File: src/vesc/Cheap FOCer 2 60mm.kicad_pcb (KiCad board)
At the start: 2 copper layers, 59.1 x 99.9 mm, 193 parts, among them J1 Conn_01x02, J2 Conn_01x07, J3 Conn_01x03, J4 On/Off, J5 UNUSED MCU PINS, J6 Conn_01x03, P1 MOTOR1, P2 MOTOR1, P3 MOTOR1, P4 HALL/Encoder, P5 SWD, Q1 NCEP60T20, Q2 NCEP60T20, Q3 NCEP60T20, Q4 NCEP60T20, Q5 NCEP60T20, Q6 NCEP60T20, U1 AMS1117-3.3, U2 DRV8301, U3 TP2604-SR, U4 TJA1051T/3/1J, U5 STM32F405RGT6, U6 BMI160, X1 8MHz 10ppm (X50328MSB2GI)

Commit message: routing
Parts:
- removed C10, C11, C9: 22uF, Capacitor_SMD:C_0805_2012Metric
- removed C20, C21, C22: 22uf, Capacitor_SMD:C_0805_2012Metric
- removed C25: 2.2uF, Capacitor_SMD:C_0603_1608Metric
- removed C43: 0.1u, Capacitor_SMD:C_0603_1608Metric
- removed C44: 1nF, Capacitor_SMD:C_0603_1608Metric
- removed C54: 2.2u, Capacitor_SMD:C_0603_1608Metric
- removed C60, C64: 100n, Capacitor_SMD:C_0603_1608Metric
- removed D1, D2: SMF05CT1G, Package_TO_SOT_SMD:SOT-363_SC-70-6
- removed D6: 100v, 1A, Diode_SMD:D_SMA
- removed H3: SLJ, shapes3D:Sam_J
- removed H7: MountingHole, MountingHole:MountingHole_3.2mm_M3_ISO14580_Pad
- removed J2: Conn_01x07, Connector_JST:JST_PH_B7B-PH-K_1x07_P2.00mm_Vertical
- removed J4: On/Off, Connector_JST:JST_PH_B2B-PH-K_1x02_P2.00mm_Vertical
- removed J5: UNUSED MCU PINS, Connector_PinHeader_2.00mm:PinHeader_2x05_P2.00mm_Vertical
- removed J6: Conn_01x03, Connector_PinHeader_2.54mm:PinHeader_1x02_P2.54mm_Vertical
- removed NEG3: MOTOR3, CRF1:1pin_4mm
- removed NTC1: NTC 10k, Resistor_SMD:R_0603_1608Metric
- removed P5: SWD, Connector_PinHeader_2.54mm:PinHeader_1x05_P2.54mm_Vertical
- removed POS1: POS, CRF1:1pin_4mm
- removed R21: 18k, Resistor_SMD:R_0603_1608Metric
- removed R40, R68, R71, R72: DNP, Resistor_SMD:R_0603_1608Metric
- removed R5, R7, R9: 100R, Resistor_SMD:R_0603_1608Metric
- removed R62, R63: 60, Resistor_SMD:R_0603_1608Metric
- removed R64, R65: 20k, Resistor_SMD:R_0603_1608Metric
- removed U4: TJA1051T/3/1J, Package_SO:SOIC-8_3.9x4.9mm_P1.27mm
- removed U6: BMI160, Package_LGA:Bosch_LGA-14_3x2.5mm_P0.5mm
- removed USB1: USB Micro U-D-M5DD-W-1, Connector_USB:USB_Micro-B_Wuerth_614105150721_Vertical
- added C201: 220n, Capacitor_SMD:C_0402_1005Metric, F.Cu at (159.6, 158.7)
- added D101: 5V, Package_TO_SOT_SMD:SOT-523, F.Cu at (156.8, 145.8)
- added D102: 5V, Package_TO_SOT_SMD:SOT-523, F.Cu at (122.5, 158.1)
- added D105: 3V3, Package_DFN_QFN:Diodes_UDFN-10_1.0x2.5mm_P0.5mm, F.Cu at (148.9, 159.1)
- added D210: 30V, Diode_SMD:D_SMF, F.Cu at (125.7, 129.9)
- added D501: 3V3, Package_DFN_QFN:Diodes_UDFN-10_1.0x2.5mm_P0.5mm, F.Cu at (121.0, 145.0)
- added D601: D_Schottky, Diode_SMD:D_SOD-123, F.Cu at (128.9, 112.4)
- added J101: USB_C_Receptacle_USB2.0_16P, Connector_USB:USB_C_Receptacle_GCT_USB4110, F.Cu at (122.3, 164.7)
- added J7: Conn_02x03_Odd_Even, Connector_PinHeader_1.27mm:PinHeader_2x03_P1.27mm_Vertical_SMD, F.Cu at (119.6, 151.6)
- added R501: 10k, Resistor_SMD:R_0402_1005Metric, F.Cu at (121.0, 141.7)
- added R73: 10k, Resistor_SMD:R_0402_1005Metric, F.Cu at (189.6, 120.9)
- added TH401: 10k, Resistor_SMD:R_0402_1005Metric, F.Cu at (124.1, 139.9)
- added U3: TCAN1462V, Package_SO:SOIC-8_3.9x4.9mm_P1.27mm, F.Cu at (156.8, 139.9)
- added U3B1: TP2604-SR, Package_SO:SOP-8_3.76x4.96mm_P1.27mm, F.Cu at (179.7, 117.2)
- added U3C1: TP2604-SR, Package_SO:SOP-8_3.76x4.96mm_P1.27mm, F.Cu at (190.6, 129.3)
- C1: value 100n -> 33n; footprint Capacitor_SMD:C_0603_1608Metric -> Capacitor_SMD:C_0402_1005Metric
- C12: value 6.8n -> 10n; footprint Capacitor_SMD:C_0603_1608Metric -> Capacitor_SMD:C_0402_1005Metric
- C13: value 120p -> 100p; footprint Capacitor_SMD:C_0603_1608Metric -> Capacitor_SMD:C_0402_1005Metric
- C14: value 15nF -> 10n; footprint Capacitor_SMD:C_0603_1608Metric -> Capacitor_SMD:C_0402_1005Metric
- C15, C31: value 4.7uF, 100V -> 4u7
- C16, C29, C33, C34, C57, C58, C61, C62, C63, C65, C66, C67: value 1nF -> 1n; footprint Capacitor_SMD:C_0603_1608Metric -> Capacitor_SMD:C_0402_1005Metric
- C18, C24, C27: value 220n -> 330n
- C19: value 2.2uF -> 22u; footprint Capacitor_SMD:C_0603_1608Metric -> Capacitor_SMD:C_1210_3225Metric
- C2: value 0.01uF -> 2u2
- C23: value 22n -> 33n
- C26: value 2.2uF -> 4u7; footprint Capacitor_SMD:C_0603_1608Metric -> Capacitor_SMD:C_1210_3225Metric
- C28: value 2.2uF -> 2u2; footprint Capacitor_SMD:C_0603_1608Metric -> Capacitor_SMD:C_1206_3216Metric
- C3: value 0.01uF -> 10u; footprint Capacitor_SMD:C_0603_1608Metric -> Capacitor_SMD:C_1206_3216Metric
- C30: value 2.2uF -> 2u2
- C32: value 100n -> 220n; footprint Capacitor_SMD:C_0603_1608Metric -> Capacitor_SMD:C_0402_1005Metric
- C35, C36, C37: value 10uF, 100V -> 4u7; footprint Capacitor_SMD:C_2220_5650Metric_Pad1.97x5.40mm_HandSolder -> Capacitor_SMD:C_1210_3225Metric
- C38, C39: value 330u, 63V -> 270u; footprint w_capacitors:CP_10x20mm_hor_with_model_brd_edge -> Capacitor_SMD:CP_Elec_10x10
- C4: value .01uF -> 220n; footprint Capacitor_SMD:C_0603_1608Metric -> Capacitor_SMD:C_0402_1005Metric
- C40, C41, C42: value 4.7nF, 100V -> 3n3; footprint Capacitor_SMD:C_0805_2012Metric -> Capacitor_SMD:C_0402_1005Metric
- C45: value 2.2u -> 4u7; footprint Capacitor_SMD:C_0603_1608Metric -> Capacitor_SMD:C_0805_2012Metric
- C46, C47, C48, C49, C53: value 2.2u -> 220n; footprint Capacitor_SMD:C_0603_1608Metric -> Capacitor_SMD:C_0402_1005Metric
- C5, C55, C56, C8: value 2.2u -> 2u2
- C50, C51: value 15p -> 10p; footprint Capacitor_SMD:C_0603_1608Metric -> Capacitor_SMD:C_0402_1005Metric
- C52, C59, C6: footprint Capacitor_SMD:C_0603_1608Metric -> Capacitor_SMD:C_0402_1005Metric
- C7: value 100n -> 10u; footprint Capacitor_SMD:C_0603_1608Metric -> Capacitor_SMD:C_1206_3216Metric
- H1, H13, H2, H5, H6, H8: footprint MountingHole:MountingHole_3.2mm_M3_ISO14580_Pad -> Bluesat:M2.5
- J1: footprint Connector_JST:JST_PH_B2B-PH-K_1x02_P2.00mm_Vertical -> Bluesat:SM02B-PASS
- J3: value Conn_01x03 -> Conn_01x02; footprint Connector_JST:JST_PH_B3B-PH-K_1x03_P2.00mm_Vertical -> Connector_AMASS:AMASS_XT30PW-M_1x02_P2.50mm_Horizontal
- L1: value 22u -> 47u; footprint Inductor_SMD:L_Taiyo-Yuden_NR-60xx_HandSoldering -> Inductor_SMD:L_Changjiang_FXL0630
- P4: footprint Connector_JST:JST_PH_B6B-PH-K_1x06_P2.00mm_Vertical -> Bluesat:BM06B-PASK
- Q1, Q2, Q3, Q4, Q5, Q6: footprint shapes3D:TO-220-3_Horizontal_TabUp_no_hole -> Package_TO_SOT_THT:TO-220-3_Horizontal_TabUp
- R1: value 39k -> 220k; footprint Resistor_SMD:R_0603_1608Metric -> Resistor_SMD:R_0402_1005Metric
- R10, R11: value 100R -> 470R; footprint Resistor_SMD:R_0603_1608Metric -> Resistor_SMD:R_0402_1005Metric
- R12, R13, R14, R15, R16, R17, R19, R20, R22, R23, R24, R25, R26, R28, R29, R3, R30, R32, R34, R35, R38, R4, R66, R67: footprint Resistor_SMD:R_0603_1608Metric -> Resistor_SMD:R_0402_1005Metric
- R18: value 3.3k -> 4k7; footprint Resistor_SMD:R_0603_1608Metric -> Resistor_SMD:R_0402_1005Metric
- R2: value 2k2 -> 10k; footprint Resistor_SMD:R_0603_1608Metric -> Resistor_SMD:R_0402_1005Metric
- R27, R31, R36: value 39k -> 47k; footprint Resistor_SMD:R_0603_1608Metric -> Resistor_SMD:R_0402_1005Metric
- R33, R37, R39, R41, R42, R43, R47, R48, R49, R53, R54, R55: footprint Resistor_SMD:R_0805_2012Metric -> Resistor_SMD:R_0402_1005Metric
- R44, R45, R46, R50, R51, R52: value 4.7k -> 4k7; footprint Resistor_SMD:R_0603_1608Metric -> Resistor_SMD:R_0402_1005Metric
- R56, R57, R58, R59, R60, R61: value 0.001R -> 1m; footprint shapes3D:R_2512_Yageo_big_pads -> Resistor_SMD:R_2512_6332Metric
- R6: value 100R -> 10k; footprint Resistor_SMD:R_0603_1608Metric -> Resistor_SMD:R_0402_1005Metric
- R69, R70: value 1k -> 10k; footprint Resistor_SMD:R_0603_1608Metric -> Resistor_SMD:R_0402_1005Metric
- R8: value 100R -> 15k; footprint Resistor_SMD:R_0603_1608Metric -> Resistor_SMD:R_0402_1005Metric
- U1: value AMS1117-3.3 -> HX4002; footprint Package_TO_SOT_SMD:SOT-223-3_TabPin2 -> Package_TO_SOT_SMD:SOT-23-6
- U3A1: renamed from U3; footprint Package_SO:SOIC-8_3.9x4.9mm_P1.27mm -> Package_SO:SOP-8_3.76x4.96mm_P1.27mm
- X1: value 8MHz 10ppm (X50328MSB2GI) -> 24MHz; footprint Crystal:Crystal_SMD_5032-2Pin_5.0x3.2mm -> Crystal:Crystal_SMD_2016-4Pin_2.0x1.6mm
- moved J3 110.8 mm to (142.6, 56.4), turned to 0 degrees
- moved R8 76.1 mm to (189.6, 114.9), turned to 0 degrees
- moved R69 69.4 mm to (189.6, 116.9), turned to 0 degrees
- moved R70 69.2 mm to (189.6, 118.9)
- moved R6 51.8 mm to (189.6, 112.9), turned to 0 degrees
- moved C2 38.9 mm to (166.1, 154.9), turned to -90 degrees
- moved C3 30.5 mm to (157.3, 154.8)
- moved C38 26.9 mm to (134.1, 84.3), turned to -90 degrees
- moved C39 24.8 mm to (154.5, 84.3), turned to -90 degrees
- moved J1 21.0 mm to (169.5, 146.7), turned to -90 degrees
- moved C4 18.8 mm to (156.9, 135.2), turned to 0 degrees
- moved C7 18.6 mm to (158.7, 150.6)
- moved C8 18.1 mm to (155.0, 159.9), turned to 180 degrees
- moved U1 16.5 mm to (161.5, 155.0), turned to 0 degrees
- moved U3A1 15.4 mm to (165.6, 136.9), turned to -90 degrees
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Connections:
- C19 pad 2: +5V -> VCC
- C2 pad 1: GND -> Net-(U1-CP+)
- C2 pad 2: /MCU/SCK_ADC_EXT -> Net-(U1-CP-)
- C3 pad 1: GND -> VCC
- C3 pad 2: /MCU/MISO_ADC_EXT2 -> GND
- C4 pad 1: GND -> Net-(U1-VOUT)
- C4 pad 2: /MCU/SERVO -> GND
- C59 pad 1: Net-(C59-Pad1) -> Net-(U3B1B-+)
- C7 pad 1: GND -> Net-(U1-VOUT)
- C7 pad 2: +5V -> GND
- J3 pad 1: GND -> V_SUPPLY
- J3 pad 2: +5V -> GND
- L1 pad 2: +5V -> VCC
- P4 pad 2: /HALL3 -> VCC
- P4 pad 3: /Filters/HALL2_IN -> /Filters/TEMP_IN
- P4 pad 5: /Filters/TEMP_IN -> /Filters/HALL2_IN
- P4 pad 6: +5V -> /HALL3
- R18 pad 1: Net-(R18-Pad1) -> Net-(U2-VSENSE)
- R3 pad 1: /MCU/USB_DP -> /MCU/USB_DM
- R34 pad 2: Net-(C59-Pad1) -> Net-(U3B1B-+)
- R35 pad 1: Net-(C59-Pad1) -> Net-(U3B1B-+)
- R4 pad 1: /MCU/USB_DM -> /MCU/USB_DP
- R6 pad 1: /MCU/SERVO -> Net-(R30-Pad2)
- R6 pad 2: Net-(J3-Pad3) -> Net-(R6-Pad2)
- R66 pad 1: Net-(R64-Pad2) -> Net-(U3A1A--)
- R69 pad 1: VCC -> Net-(R6-Pad2)
- R69 pad 2: PA15 -> Net-(U3A1A--)
- R70 pad 1: PB2 -> Net-(U3B1B--)
- R70 pad 2: VCC -> Net-(R70-Pad2)
- R8 pad 1: /MCU/TX_SCL_MOSI -> VCC
- R8 pad 2: /TX_SCL_MOSI_IN -> Net-(U2-VSENSE)
- U1 pad 1: GND -> Net-(U1-VOUT)
- U1 pad 2: VCC -> GND
- U1 pad 3: +5V -> VCC
- U2 pad 12: Net-(U2-Pad12) -> unconnected-(U2-DC_CAL-Pad12)
- U2 pad 3: Net-(R18-Pad1) -> Net-(U2-VSENSE)
- U2 pad 4: Net-(U2-Pad4) -> unconnected-(U2-PWRGD-Pad4)
- U2 pad 5: Net-(U2-Pad5) -> unconnected-(U2-OCTW-Pad5)
- U2 pad 55: Net-(J4-Pad1) -> unconnected-(U2-EN_BUCK-Pad55)
- U3A1 pad 2: Net-(R64-Pad2) -> Net-(U3A1A--)
- U3A1 pad 4: GND -> (no net)
- U3A1 pad 5: Net-(C59-Pad1) -> (no net)
- U3A1 pad 6: Net-(R65-Pad1) -> (no net)
- U3A1 pad 7: Net-(R65-Pad1) -> (no net)
- U3A1 pad 8: VCC -> (no net)
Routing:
- net +5V: track 181.2 -> 0.00 mm, vias 4 -> 0
- net Net-(J4-Pad1): track 129.7 -> 0.00 mm, vias 1 -> 0
- net VCC: track 358.3 -> 234.8 mm
- net PA15: track 53.7 -> 0.00 mm, vias 1 -> 0
- net V_SUPPLY: track 143.5 -> 90.0 mm, vias 75 -> 59
- net /MCU/ADC_TEMP: track 70.0 -> 16.7 mm, vias 11 -> 10
- net /MCU/SENS2: track 60.9 -> 11.9 mm, vias 4 -> 0
- net /MCU/L3: track 44.4 -> 0.00 mm, vias 2 -> 0
- net PB2: track 38.3 -> 0.00 mm, vias 3 -> 0
- net PC14: track 38.0 -> 0.00 mm
- net PC13: track 37.2 -> 0.00 mm
- net PB4: track 37.1 -> 0.00 mm, vias 1 -> 0
- net /MCU/SDI: track 37.0 -> 0.00 mm, vias 4 -> 0
- net PC15: track 34.1 -> 0.00 mm
- net PD2: track 34.0 -> 0.00 mm, vias 1 -> 0
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- added copper zone on F.Cu, net /HALL3
- removed copper zone on F.Cu, net +5V
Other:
- board text removed: "5V"
- board text removed: "ADC1"
- board text removed: "ADC2"
- board text removed: "CAN"
- board text removed: "COMM"
- board text removed: "GND"
- board text removed: "IMU"
- board text removed: "NRST"
- board text removed: "ON"
- board text removed: "ON/OFF"
- board text removed: "PD"
- board text removed: "PU"
- board text removed: "SERVO"
- board text removed: "SWCLK"
- board text removed: "SWDIO"
- board text removed: "USB"
- board text removed: "VCC"

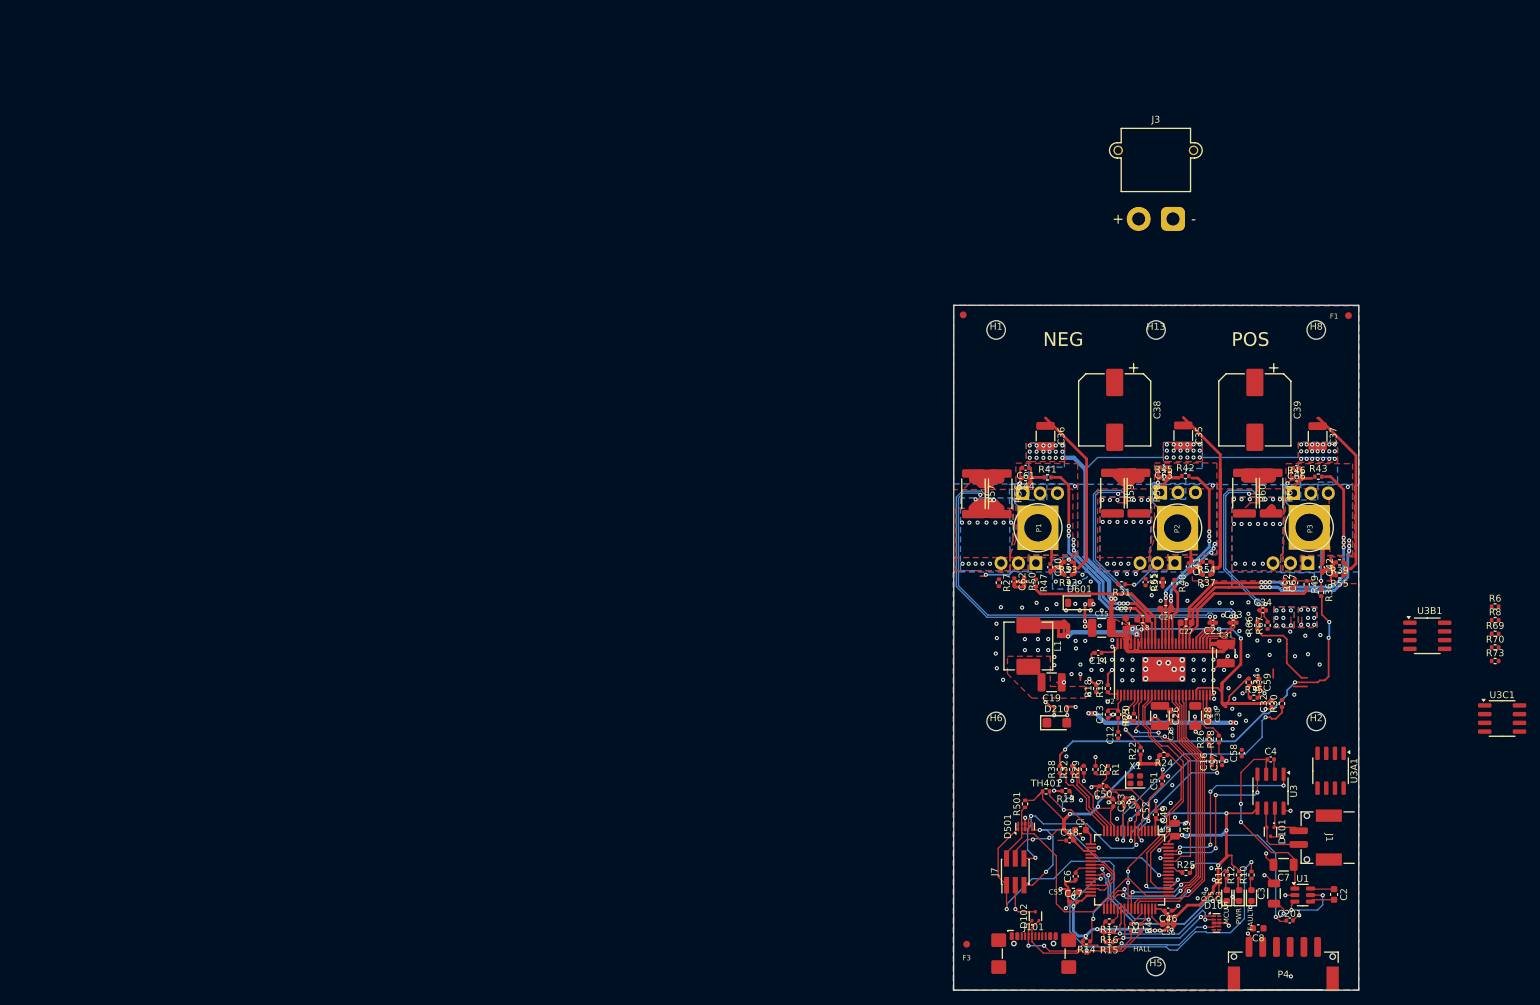
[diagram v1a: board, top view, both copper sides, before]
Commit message: component placement
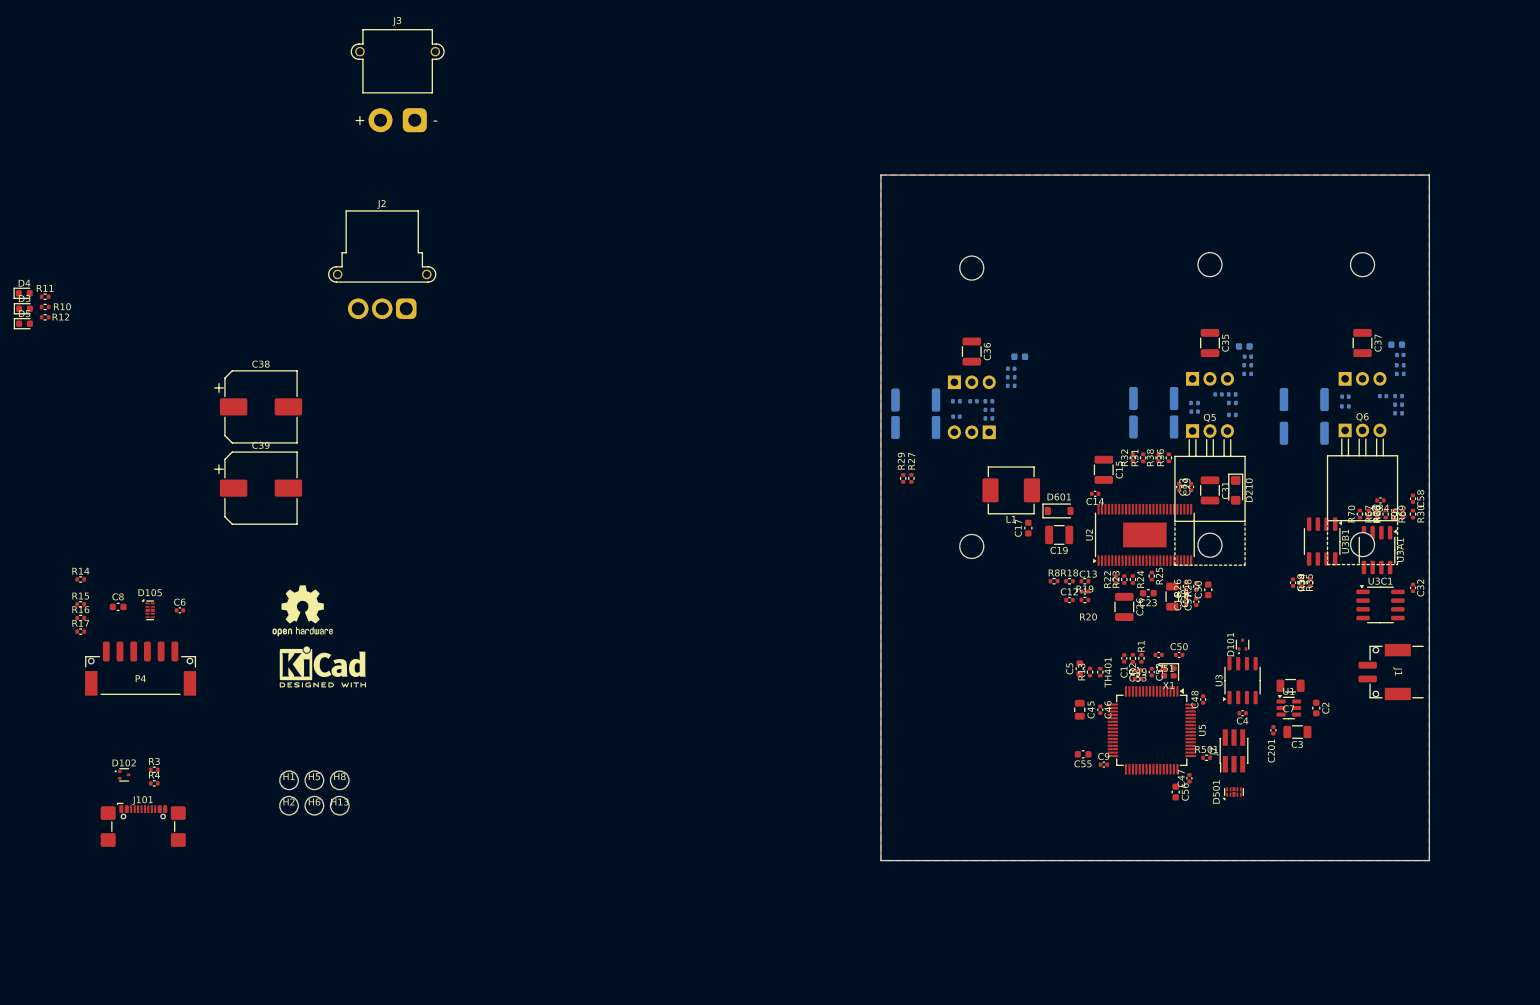
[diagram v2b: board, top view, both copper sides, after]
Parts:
- removed F1, F2, F3: Fiducial, Fiducial:Fiducial_1mm_Dia_2mm_Outer
- removed NT1, NT2, NT3, NT4, NT5, NT6: Net-Tie_2, NetTie:NetTie-2_SMD_Pad0.5mm
- removed P1, P2, P3: MOTOR1, CRF1:1pin_4mm
- added C9: 220n, Capacitor_SMD:C_0402_1005Metric, F.Cu at (132.5, 136.0)
- added J2: Conn_01x03, Connector_AMASS:AMASS_MR30PW-FB_1x03_P3.50mm_Horizontal, F.Cu at (30.8, 69.5)
- C18, C24, C27, C40, C41, C42, C61, C62, C63, C65, C66, C67, R33, R37, R39, R41, R42, R43, R44, R45, R46, R47, R48, R49, R50, R51, R52, R53, R54, R55, R56, R57, R58, R59, R60, R61: moved to B.Cu
- H4, H9, Q5, Q6: moved to F.Cu
- moved D3 198.4 mm to (-24.9, 69.5), turned to 0 degrees
- moved D4 196.2 mm to (-25.0, 67.2), turned to 0 degrees
- moved D5 195.8 mm to (-24.9, 71.7), turned to 0 degrees
- moved R10 194.5 mm to (-21.9, 69.2), turned to 0 degrees
- moved R12 192.2 mm to (-21.9, 70.8), turned to 0 degrees
- moved R11 191.9 mm to (-21.9, 67.8), turned to 0 degrees
- moved C8 172.8 mm to (-11.3, 113.0), turned to 0 degrees
- moved P4 172.2 mm to (-8.00, 119.5)
- moved D105 162.1 mm to (-6.61, 113.5)
- moved R15 157.9 mm to (-16.7, 112.6), turned to 0 degrees
- moved R16 156.9 mm to (-16.7, 114.6), turned to 0 degrees
- moved H8 156.9 mm to (21.1, 138.3)
- moved R14 155.9 mm to (-16.7, 109.0), turned to 0 degrees
- moved R17 155.9 mm to (-16.7, 116.6), turned to 0 degrees
- moved H4 151.8 mm to (15.6, 113.6), turned to 0 degrees
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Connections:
- C1 pad 1: GND -> SPA
- C12 pad 1: GND -> SPA
- C13 pad 1: GND -> SPA
- C14 pad 2: GND -> SPA
- C15 pad 1: GND -> SPA
- C16 pad 1: GND -> SPA
- C19 pad 1: GND -> SPA
- C201 pad 2: GND -> SPA
- C26 pad 2: GND -> SPA
- C28 pad 2: GND -> SPA
- C3 pad 2: GND -> SPA
- C30 pad 1: GND -> SPA
- C31 pad 1: GND -> SPA
- C32 pad 1: GND -> SPA
- C33 pad 2: SPB -> SPA
- C34 pad 2: SPC -> SPA
- C35 pad 1: GND -> SPA
- C36 pad 1: GND -> SPA
- C37 pad 1: GND -> SPA
- C38 pad 2: GND -> SPA
- C39 pad 2: GND -> SPA
- C4 pad 2: GND -> SPA
- C45 pad 1: GND -> SPA
- C46 pad 1: GND -> SPA
- C47 pad 1: GND -> SPA
- C48 pad 1: GND -> SPA
- C49 pad 1: GND -> SPA
- C5 pad 2: GND -> SPA
- C50 pad 2: GND -> SPA
- C51 pad 2: GND -> SPA
- C52 pad 1: GND -> SPA
- C53 pad 1: GND -> SPA
- C55 pad 2: GND -> SPA
- C56 pad 2: GND -> SPA
- C57 pad 1: GND -> SPA
- C58 pad 1: GND -> SPA
- C59 pad 2: GND -> SPA
- C6 pad 1: GND -> SPA
- C62 pad 2: /Mosfet driver/H1_LOW -> SNA
- C65 pad 2: /Mosfet driver/H2_LOW -> SNB
- C67 pad 2: /Mosfet driver/H3_LOW -> SNC
- C7 pad 2: GND -> SPA
- C8 pad 2: GND -> SPA
- D101 pad 3: GND -> SPA
- D102 pad 3: GND -> SPA
- D105 pad 3: GND -> SPA
- D105 pad 8: GND -> SPA
- D210 pad 1: GND -> SPA
- D3 pad 1: GND -> SPA
- D4 pad 1: GND -> SPA
- D5 pad 1: GND -> SPA
- D501 pad 3: GND -> SPA
- D501 pad 8: GND -> SPA
- D601 pad 2: GND -> SPA
- J101 pad A1: GND -> SPA
- J101 pad A12: GND -> SPA
- J101 pad B1: GND -> SPA
- J101 pad B12: GND -> SPA
- J101 pad S1: GND -> SPA
- J3 pad 2: GND -> SPA
- J7 pad 3: GND -> SPA
- P4 pad 1: GND -> SPA
- Q4 pad 3: /Mosfet driver/H1_LOW -> SNA
- Q5 pad 3: /Mosfet driver/H2_LOW -> SNB
- Q6 pad 3: /Mosfet driver/H3_LOW -> SNC
- R13 pad 2: GND -> SPA
- R18 pad 2: GND -> SPA
- R19 pad 2: GND -> SPA
- R2 pad 1: GND -> SPA
- R23 pad 1: GND -> SPA
- R29 pad 1: GND -> SPA
- R32 pad 1: GND -> SPA
- R33 pad 1: GND -> SPA
- R35 pad 2: GND -> SPA
- R37 pad 1: GND -> SPA
- R38 pad 1: GND -> SPA
- R39 pad 1: GND -> SPA
- R50 pad 2: /Mosfet driver/H1_LOW -> SNA
- R51 pad 1: /Mosfet driver/H2_LOW -> SNB
- R52 pad 1: /Mosfet driver/H3_LOW -> SNC
- R53 pad 1: GND -> SPA
- R54 pad 1: GND -> SPA
- R55 pad 1: GND -> SPA
- R56 pad 1: GND -> SPA
- R56 pad 2: /Mosfet driver/H1_LOW -> SNA
- R57 pad 1: GND -> SPA
- R57 pad 2: /Mosfet driver/H1_LOW -> SNA
- R58 pad 1: GND -> SPA
- R58 pad 2: /Mosfet driver/H2_LOW -> SNB
- R59 pad 1: GND -> SPA
- R59 pad 2: /Mosfet driver/H2_LOW -> SNB
- R60 pad 1: GND -> SPA
- R60 pad 2: /Mosfet driver/H3_LOW -> SNC
- R61 pad 1: GND -> SPA
- R61 pad 2: /Mosfet driver/H3_LOW -> SNC
- R67 pad 2: SPC -> SPA
- U1 pad 2: GND -> SPA
- U2 pad 28: GND -> SPA
- U2 pad 30: SPB -> SPA
- U2 pad 34: /Mosfet driver/H3_LOW -> SNC
- U2 pad 39: /Mosfet driver/H2_LOW -> SNB
- U2 pad 44: /Mosfet driver/H1_LOW -> SNA
- U2 pad 57: GND -> SPA
- U3 pad 2: GND -> SPA
- U3 pad 8: GND -> SPA
- U3C1 pad 4: GND -> SPA
- U5 pad 12: GND -> SPA
- U5 pad 18: GND -> SPA
- U5 pad 60: GND -> SPA
- U5 pad 63: GND -> SPA
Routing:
- net VCC: track 234.8 -> 0.00 mm, vias 31 -> 0
- net GND: track 216.6 -> 0.00 mm, vias 184 -> 0
- net V_SUPPLY: track 90.0 -> 0.00 mm, vias 59 -> 0
- net /Mosfet driver/H3_VS: track 80.5 -> 0.00 mm, vias 9 -> 0
- net /MCU/SENS3: track 70.4 -> 0.00 mm, vias 4 -> 0
- net SPA: track 62.7 -> 0.00 mm, vias 2 -> 0
- net SNA: track 62.5 -> 0.00 mm, vias 2 -> 0
- net /Mosfet driver/H1_VS: track 52.5 -> 0.00 mm, vias 9 -> 0
- net /Mosfet driver/GH_C: track 52.2 -> 0.00 mm, vias 6 -> 0
- net /MCU/LED_RED: track 50.1 -> 0.00 mm, vias 2 -> 0
- net SNB: track 46.8 -> 0.00 mm, vias 2 -> 0
- net SWDIO: track 46.1 -> 0.00 mm, vias 2 -> 0
- net SPB: track 45.7 -> 0.00 mm, vias 2 -> 0
- net /Mosfet driver/H2_VS: track 45.6 -> 0.00 mm, vias 8 -> 0
- net /MCU/L1: track 44.8 -> 0.00 mm, vias 2 -> 0
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- added copper zone on In1.Cu, net SPA
- added copper zone on In4.Cu, net SPA
- removed copper zone on F.Cu, net /HALL3
- removed copper zone on B.Cu, net /MCU/ADC_TEMP
- removed copper zone on F.Cu, net /MCU/ADC_TEMP
- removed copper zone on B.Cu, net /Mosfet driver/H1_LOW
- removed copper zone on F.Cu, net /Mosfet driver/H1_LOW
- removed copper zone on B.Cu, net /Mosfet driver/H1_VS
- removed copper zone on F.Cu, net /Mosfet driver/H1_VS
- removed copper zone on B.Cu, net /Mosfet driver/H2_LOW
- removed copper zone on F.Cu, net /Mosfet driver/H2_LOW
- removed copper zone on B.Cu, net /Mosfet driver/H2_VS
- removed copper zone on F.Cu, net /Mosfet driver/H2_VS
- removed copper zone on B.Cu, net /Mosfet driver/H3_LOW
- removed copper zone on F.Cu, net /Mosfet driver/H3_LOW
- removed copper zone on B.Cu, net /Mosfet driver/H3_VS
- removed copper zone on F.Cu, net /Mosfet driver/H3_VS
- removed copper zone on B.Cu, net GND
- removed copper zone on F.Cu, net GND
- removed copper zone on F.Cu, net Net-(D601-K)
- removed copper zone on B.Cu, net VCC
- removed copper zone on F.Cu, net VCC
- removed copper zone on B.Cu, net V_SUPPLY
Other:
- board size 59.1 x 99.9 mm -> 80 x 100 mm
- copper layers 2 -> 6
- board text removed: "CHEAP FOCER 2"
- board text removed: "FAULT"
- board text removed: "HALL"
- board text removed: "MCU"
- board text removed: "NEG"
- board text removed: "POS"
- board text removed: "PWR"
